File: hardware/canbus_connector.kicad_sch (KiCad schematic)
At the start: 2 parts, among them J2 RJ45, J3 RJ45

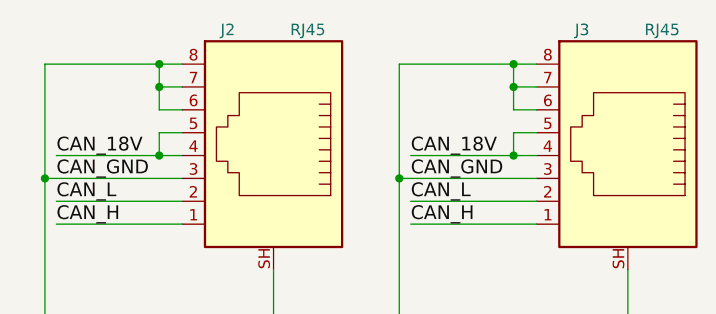
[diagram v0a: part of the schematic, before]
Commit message: Troca do atmega328p -> STM32F103C8T Já que tem CAN integrado e ADC 12 bits (ao invés de 10)
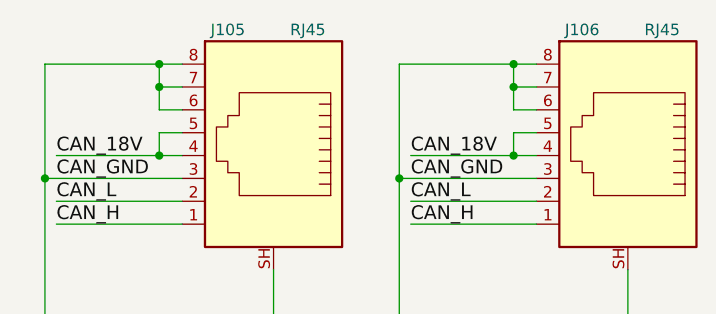
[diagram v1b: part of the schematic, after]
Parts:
- renumbered J2 to J105, J3 to J106
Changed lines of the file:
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@@
   (symbol (lib_id "Connector:RJ45_Shielded") (at 190.5 86.36 0) (mirror y) (unit 1)
     (in_bom yes) (on_board yes)
-    (property "Reference" "J3" (id 0) (at 185.42 72.39 0))
+    (property "Reference" "J106" (id 0) (at 185.42 72.39 0))
     (property "Value" "RJ45" (id 1) (at 194.31 72.39 0))
     (property "Footprint" "KicadZeniteSolarLibrary18:RJ45_YH59_01" (id 2) (at 190.5 86.36 0)
@@
   (symbol (lib_id "Connector:RJ45_Shielded") (at 151.13 86.36 0) (mirror y) (unit 1)
     (in_bom yes) (on_board yes)
-    (property "Reference" "J2" (id 0) (at 146.05 72.39 0))
+    (property "Reference" "J105" (id 0) (at 146.05 72.39 0))
     (property "Value" "RJ45" (id 1) (at 154.94 72.39 0))
     (property "Footprint" "KicadZeniteSolarLibrary18:RJ45_YH59_01" (id 2) (at 151.13 86.36 0)
@@
   (symbol (lib_id "power:GND") (at 125.73 116.84 0) (unit 1)
     (in_bom yes) (on_board yes)
-    (property "Reference" "#PWR036" (id 0) (at 125.73 123.19 0)
+    (property "Reference" "#PWR0144" (id 0) (at 125.73 123.19 0)
       (effects (font (size 1.27 1.27)) hide)
     )
@@
   (symbol (lib_id "power:GND") (at 81.28 96.52 0) (unit 1)
     (in_bom yes) (on_board yes)
-    (property "Reference" "#PWR035" (id 0) (at 81.28 102.87 0)
+    (property "Reference" "#PWR0143" (id 0) (at 81.28 102.87 0)
       (effects (font (size 1.27 1.27)) hide)
     )

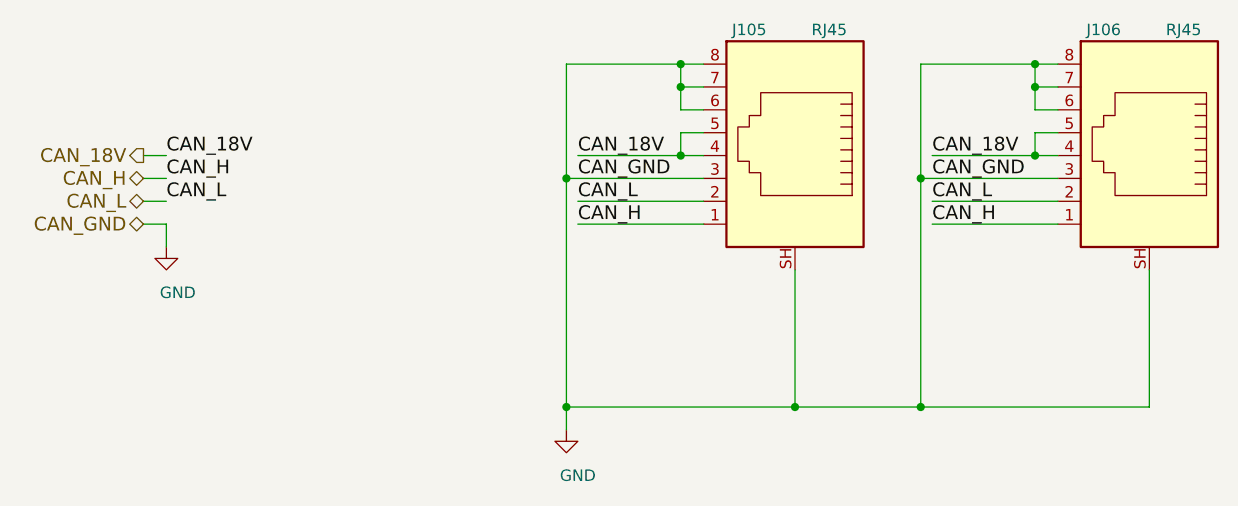
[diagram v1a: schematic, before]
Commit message: hardware: fixed RJ45 footp sh pin, added shapes3D (including K78L15)
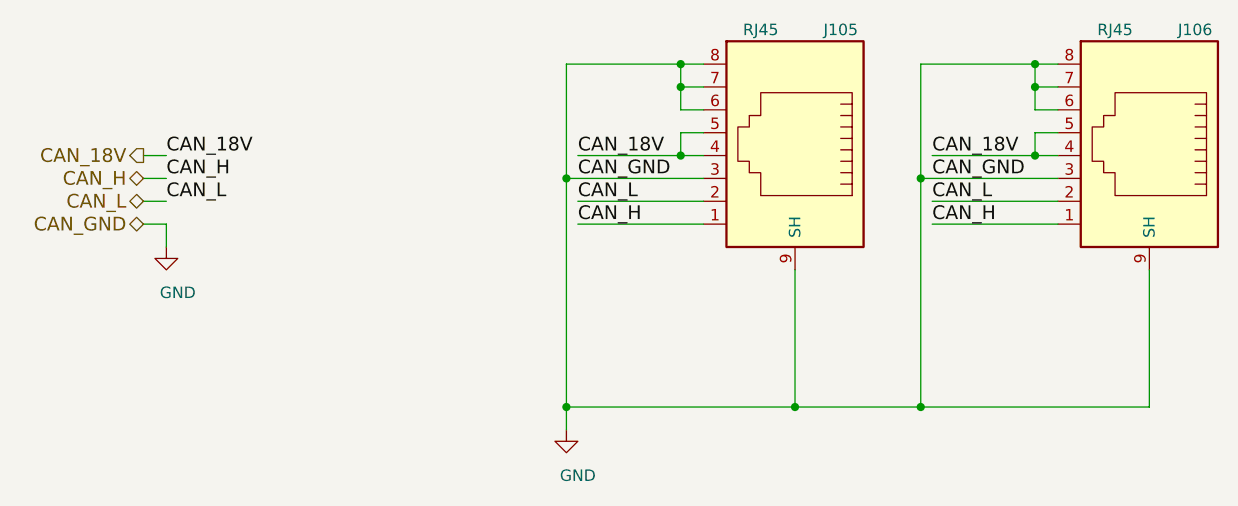
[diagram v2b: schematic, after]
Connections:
- net GND: now also J105.9 (SH), J106.9 (SH); no longer J105.SH, J106.SH
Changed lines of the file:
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@@
   (symbol (lib_id "Connector:RJ45_Shielded") (at 190.5 86.36 0) (mirror y) (unit 1)
     (in_bom yes) (on_board yes)
-    (property "Reference" "J106" (id 0) (at 185.42 72.39 0))
-    (property "Value" "RJ45" (id 1) (at 194.31 72.39 0))
+    (property "Reference" "J106" (id 0) (at 195.58 72.39 0))
+    (property "Value" "RJ45" (id 1) (at 186.69 72.39 0))
     (property "Footprint" "KicadZeniteSolarLibrary18:RJ45_YH59_01" (id 2) (at 190.5 86.36 0)
       (effects (font (size 1.27 1.27)) hide)
@@
     (pin "7")
     (pin "8")
-    (pin "SH")
+    (pin "9")
   )
-  (symbol (lib_id "Connector:RJ45_Shielded") (at 151.13 86.36 0) (mirror y) (unit 1)
+  (symbol (lib_name "RJ45_Shielded_1") (lib_id "Connector:RJ45_Shielded") (at 151.13 86.36 0) (mirror y) (unit 1)
     (in_bom yes) (on_board yes)
-    (property "Reference" "J105" (id 0) (at 146.05 72.39 0))
-    (property "Value" "RJ45" (id 1) (at 154.94 72.39 0))
+    (property "Reference" "J105" (id 0) (at 156.21 72.39 0))
+    (property "Value" "RJ45" (id 1) (at 147.32 72.39 0))
     (property "Footprint" "KicadZeniteSolarLibrary18:RJ45_YH59_01" (id 2) (at 151.13 86.36 0)
       (effects (font (size 1.27 1.27)) hide)
@@
     (pin "7")
     (pin "8")
-    (pin "SH")
+    (pin "9")
   )
   (symbol (lib_id "power:GND") (at 125.73 116.84 0) (unit 1)
